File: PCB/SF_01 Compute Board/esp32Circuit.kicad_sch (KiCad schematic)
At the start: 62 parts, among them J16 USB_C_Receptacle_USB2.0_16P, J3 UART, J4 JTAG, SW3 ESP_BOOT, SW4 ESP_RESET, U10 TPD4E02B04DQA, U11 LP5907MFX-3.3, U12 74LVC2G53, U13 74LVC2G53, U14 PCM5102A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

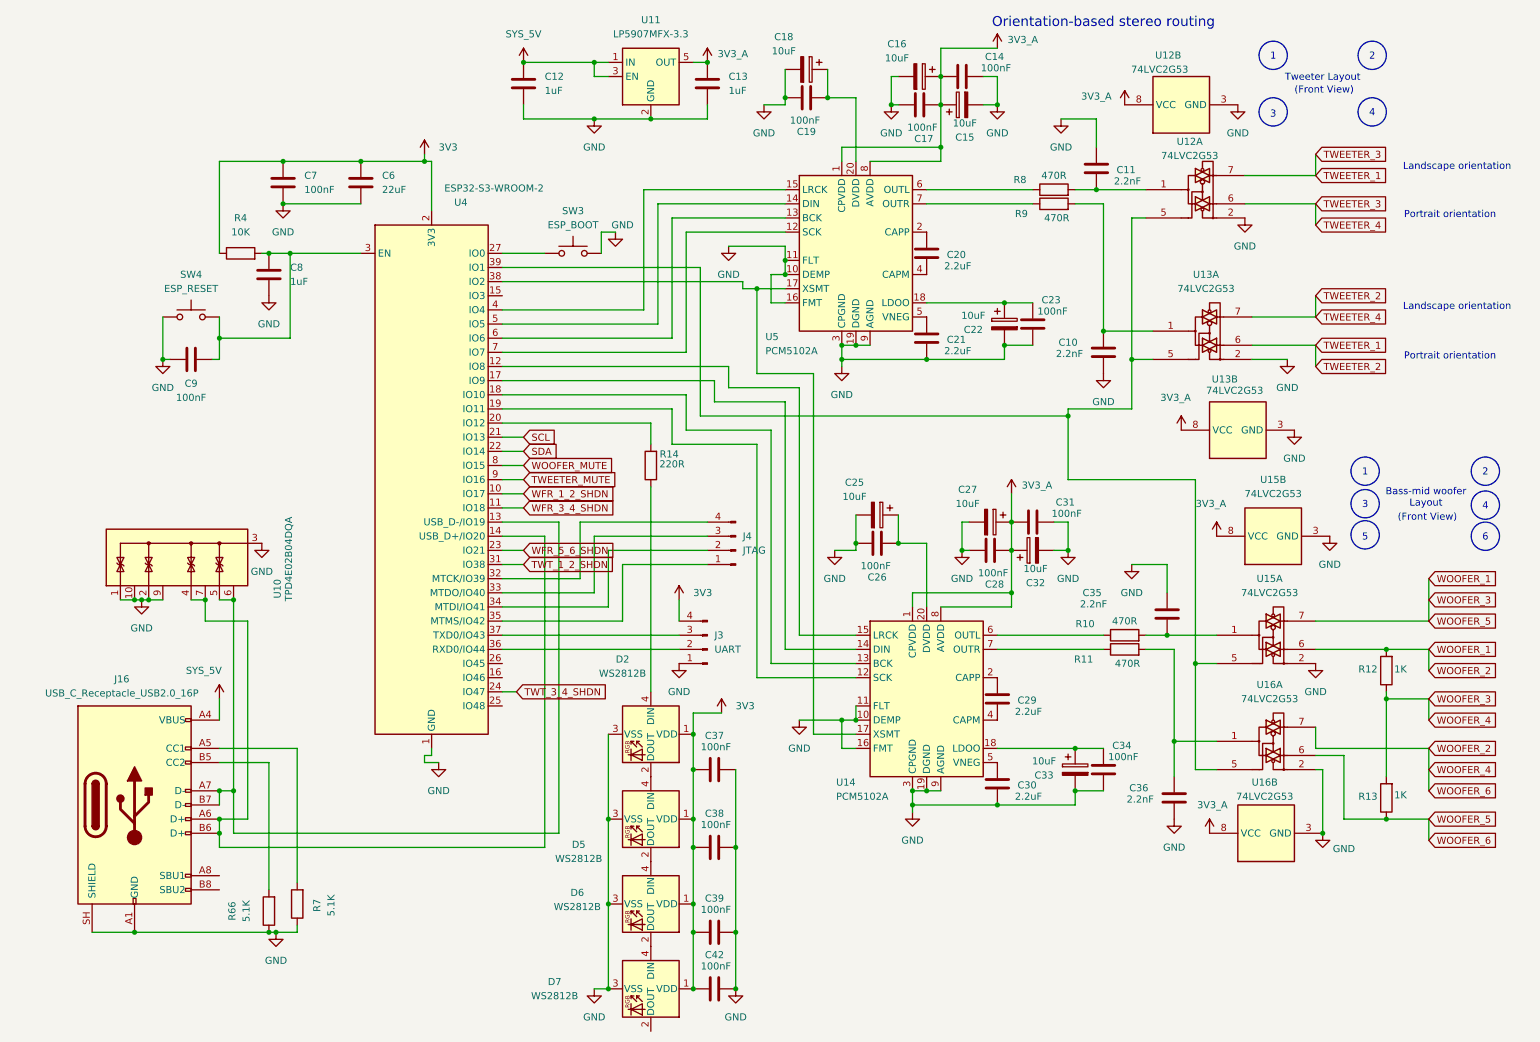
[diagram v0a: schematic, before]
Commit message: Changed Audio Multiplexer Circuit, Routed more
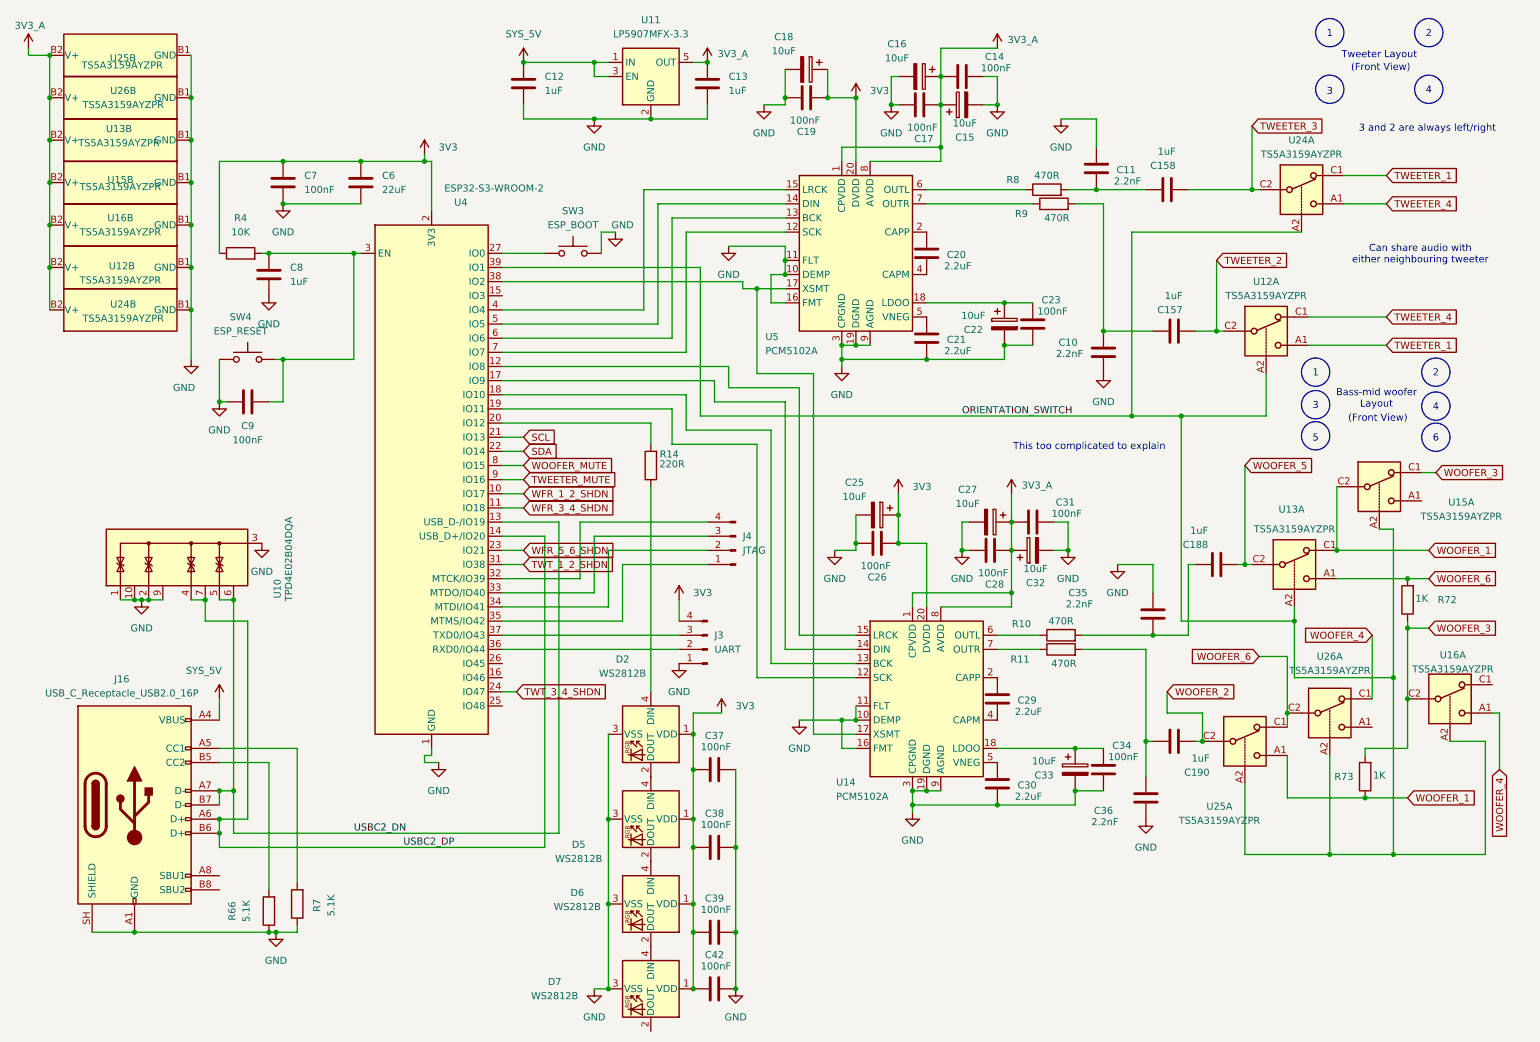
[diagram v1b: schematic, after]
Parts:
- removed R12, R13: 1K, Resistor_SMD:R_0603_1608Metric, symbol Device:R
- removed U12, U13, U15, U16: 74LVC2G53, Package_SO:VSSOP-8_2.3x2mm_P0.5mm, symbol 74xGxx:74LVC2G53
- added C157, C158, C188, C190: 1uF, Capacitor_SMD:C_0603_1608Metric, symbol Device:C
- added R72, R73: 1K, Resistor_SMD:R_0603_1608Metric, symbol Device:R
- added U12, U13, U15, U16, U24, U25, U26: TS5A3159AYZPR, Package_BGA:Texas_DSBGA-6_0.9x1.4mm_Layout2x3_P0.5mm, symbol Analog_Switch:TS5A3159AYZPR
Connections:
- net 3V3: now also C18.1, C19.2, C25.1, C26.2, U14.20 (DVDD), U5.20 (DVDD)
- net 3V3_A: now also U12.B2 (V+), U13.B2 (V+), U15.B2 (V+), U16.B2 (V+), U24.B2 (V+), U25.B2 (V+), U26.B2 (V+)
- net GND: now also U12.B1 (GND), U13.B1 (GND), U15.B1 (GND), U16.B1 (GND), U24.B1 (GND), U25.B1 (GND), U26.B1 (GND)
- net TWEETER_1: now also U12.A1, U24.C1
- net WOOFER_1: now also R73.1, U13.C1, U15.C2, U25.A1
- net at C36.1, R11.2: now also C190.1
- net ORIENTATION_SWITCH: now reaches U4.39 (IO1)
- net ORIENTATION_SWITCH: now also U12.A2, U13.A2, U15.A2, U16.A2, U24.A2, U25.A2, U26.A2
- net at C35.2, R10.2: now also C188.1
- net USBC2_DP: now reaches J16.A6 (D+), J16.B6 (D+), U10.4 (IO3), U10.7 (NC), U4.14 (USB_D+/IO20)
- net USBC2_DN: now reaches J16.A7 (D-), J16.B7 (D-), U10.5 (IO4), U10.6 (NC), U4.13 (USB_D-/IO19)
- net at C11.2, R8.2: now also C158.1
- net at C10.1, R9.2: now also C157.1
- new net TWEETER_2: C157.2, U12.C2
- new net TWEETER_3: C158.2, U24.C2
- new net TWEETER_4: U12.C1, U24.A1
- new net WOOFER_2: C190.2, U25.C2
- new net WOOFER_3: R72.1, R73.2, U15.C1, U16.C2
- new net WOOFER_4: U16.A1, U26.C1
- new net WOOFER_5: C188.2, U13.C2
- new net WOOFER_6: R72.2, U13.A1, U25.C1, U26.C2
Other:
- note added: "3 and 2 are always left/right"
- note added: "Can share audio with either neighbouring tweeter"
- note added: "This too complicated to explain"
- note removed: "Landscape orientation"
- note removed: "Orientation-based stereo routing"
- note removed: "Portrait orientation"
- moved on the sheet: C35, C36, C9, R10, R11, R8, SW4

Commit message: Added USB Host control, Routed 1st amplifier
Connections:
- net SYS_5V: no longer J16.A4 (VBUS), J16.A9 (VBUS), J16.B4 (VBUS), J16.B9 (VBUS)
- new net: J16.A4 (VBUS), J16.A9 (VBUS), J16.B4 (VBUS), J16.B9 (VBUS)
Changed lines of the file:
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@@
 	(wire
 		(pts
-			(xy 52.07 135.89) (xy 52.07 139.7)
-		)
-		(stroke
-			(width 0)
-			(type default)
-		)
-	)
-	(wire
-		(pts
 			(xy 137.16 172.72) (xy 137.16 177.8)
 		)
@@
 					(unit 1)
 				)
-			)
-		)
-	)
-	(symbol
-		(lib_id "power:VCC")
-		(at 52.07 135.89 0)
-		(unit 1)
-		(body_style 1)
-		(exclude_from_sim no)
-		(in_bom yes)
-		(on_board yes)
-		(in_pos_files yes)
-		(dnp no)
-		(property "Reference" "#PWR082"
-			(at 52.07 139.7 0)
-			(hide yes)
-			(show_name no)
-			(do_not_autoplace no)
-			(effects
-				(font
-					(size 1.27 1.27)
-				)
-			)
-		)
-		(property "Value" "SYS_5V"
-			(at 49.276 130.81 0)
-			(show_name no)
-			(do_not_autoplace no)
-			(effects
-				(font
-					(size 1.27 1.27)
-				)
-			)
-		)
-		(property "Footprint" ""
-			(at 52.07 135.89 0)
-			(hide yes)
-			(show_name no)
-			(do_not_autoplace no)
-			(effects
-				(font
-					(size 1.27 1.27)
-				)
-			)
-		)
-		(property "Datasheet" ""
-			(at 52.07 135.89 0)
-			(hide yes)
-			(show_name no)
-			(do_not_autoplace no)
-			(effects
-				(font
-					(size 1.27 1.27)
-				)
-			)
-		)
-		(property "Description" "Power symbol creates a global label with name \"VCC\""
-			(at 52.07 135.89 0)
-			(hide yes)
-			(show_name no)
-			(do_not_autoplace no)
-			(effects
-				(font
-					(size 1.27 1.27)
-				)
-			)
-		)
-		(pin "1"
-		)
-		(instances
-			(project "SF_01 Compute Board"
-				(path "/92cc60e0-eea7-49a8-8acb-7ee37df4a56f/9ef467e3-867c-4e70-a655-081007eb82a8"
-					(reference "#PWR082")
-					(unit 1)
-				)
